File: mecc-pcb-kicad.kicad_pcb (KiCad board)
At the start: 2 copper layers, 230.1 x 130 mm, 51 parts, among them J1 UI BUS, J2 STM SIGS, J3 Wave_Gauge, J4 4.9V, J6 VESC IN, J7 IV Sens, Q1 NMOS, Q2 NMOS, Q3 PMOS, Q4 PMOS, U1 SEN-16407

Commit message: merged with Nathan's branch
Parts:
- added C1: 100 uF, Capacitor_THT:CP_Axial_L11.0mm_D5.0mm_P18.00mm_Horizontal, F.Cu at (200.9, 108.0)
- added C2: 47 uF, Capacitor_THT:CP_Axial_L11.0mm_D5.0mm_P18.00mm_Horizontal, F.Cu at (127.9, 148.6)
- added D1: 1N4007, Diode_THT:D_DO-41_SOD81_P10.16mm_Horizontal, F.Cu at (172.7, 127.0)
- added J1: UI BUS, Connector_Molex:Molex_KK-254_AE-6410-05A_1x05_P2.54mm_Vertical, F.Cu at (142.2, 119.4)
- added J2: VBatt -> 5V, Package_SIP:SIP-8_19x3mm_P2.54mm, F.Cu at (195.6, 99.1)
- added J4: 5V -> 3.3V, Package_SIP:SIP-8_19x3mm_P2.54mm, F.Cu at (195.6, 88.9)
- added J5: PDQE15-Q48-D24-D, PDQE15-Q48-D24-D:CONV_PDQE15-Q48-D24-D, F.Cu at (109.8, 179.8)
- added J8: Torq_SENS, Connector_Molex:Molex_KK-254_AE-6410-04A_1x04_P2.54mm_Vertical, F.Cu at (97.8, 148.6)
- added R1: 3k, Resistor_THT:R_Axial_DIN0204_L3.6mm_D1.6mm_P7.62mm_Horizontal, F.Cu at (97.8, 142.2)
- added R10: 50k, Resistor_THT:R_Axial_DIN0204_L3.6mm_D1.6mm_P7.62mm_Horizontal, F.Cu at (97.8, 130.8)
- added R2: 3k, Resistor_THT:R_Axial_DIN0204_L3.6mm_D1.6mm_P7.62mm_Horizontal, F.Cu at (101.6, 134.6)
- added R9: 100k, Resistor_THT:R_Axial_DIN0204_L3.6mm_D1.6mm_P7.62mm_Horizontal, F.Cu at (101.6, 123.2)
- added U2: SN74HCS09QPWRQ1, SN74HCS09QPWRQ1:SO14_PW_TEX, F.Cu at (100.3, 196.7)
- added U3: SN74LVC1G139DCUR, SN74LVC1G139DCUR:DCU0008A_N, F.Cu at (107.7, 195.1)
- J3: footprint Connector_Molex:Molex_KK-254_AE-6410-08A_1x08_P2.54mm_Vertical -> Connector_RJ:RJ45_Amphenol_RJHSE538X
- R3: value 9.8K -> 10k
- R4: value 3.9K -> 5k
- R5: value 7.45K -> 10k
- R6: value 9K -> 27k
- R7: value 6.57K -> 4.7k
- R8: value 9.8K -> 4.7k
- RHIGH_10k1, RHIGH_10k2, RHIGH_10k3, RHIGH_10k4, RHIGH_10k5, RHIGH_10k6, R_RELAY_PULLDOWN1, R_RELAY_PULLDOWN3, R_RELAY_PULLDOWN4: footprint Resistor_THT:R_Box_L14.0mm_W5.0mm_P9.00mm -> Resistor_THT:R_Axial_DIN0204_L3.6mm_D1.6mm_P7.62mm_Horizontal
- moved J7 111.9 mm to (109.2, 88.9), turned to 0 degrees
- moved R6 105.4 mm to (101.6, 86.4), turned to -90 degrees
- moved J1 98.4 mm to (153.2, 119.4)
- moved R8 65.3 mm to (120.7, 130.8)
- moved J4 65.0 mm to (120.7, 137.2), turned to 0 degrees
- moved J3 61.3 mm to (85.5, 143.8), turned to 90 degrees
- moved R3 60.5 mm to (105.4, 123.2)
- moved TP7 43.9 mm to (113.0, 137.2)
- moved JP2 43.4 mm to (124.5, 99.1), turned to -90 degrees
- moved R7 43.2 mm to (116.8, 130.8), turned to 90 degrees
- moved R4 40.5 mm to (109.2, 130.8), turned to 90 degrees
- moved R5 39.9 mm to (113.0, 130.8), turned to 90 degrees
- moved J6 38.1 mm to (83.8, 127.0)
- moved J2 19.3 mm to (142.2, 134.6)
- moved TP8 19.3 mm to (133.7, 141.7)
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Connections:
- net TORQUE_SENSOR renamed /A0
- JP2 pad 5: IO_LOW_OUT -> LOW_OUT
- JP2 pad 6: IO_HIGH_SIDE_RELAY -> HIGH_IN
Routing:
- net +5V: track 59.7 -> 207.9 mm
- net BATT_POS: track 63.2 -> 182.0 mm
- net HIGH_SIDE_STM: track 24.9 -> 133.1 mm, vias 0 -> 2
- net PRE_LOW_DIS_STM: track 52.9 -> 149.8 mm
- net IO_HIGH_SIDE_RELAY: track 78.5 -> 0.00 mm
- net IO_LOW_OUT: track 71.9 -> 0.00 mm
- net /A3: track 87.3 -> 28.5 mm
- net GND: track 748.4 -> 806.2 mm
- net VESC_OUTPUT: track 43.5 -> 92.3 mm
- net HIGH_SIDE: track 92.4 -> 46.8 mm
- net VESC_INPUT: track 43.5 -> 83.3 mm
- net HIGH_IN: track 0.00 -> 35.7 mm
- net IO_ESTOP: track 74.4 -> 40.5 mm
- net PRE_LOW_DIS: track 162.3 -> 195.1 mm
- net LOW_OUT: track 0.00 -> 32.1 mm
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- removed copper zone on B.Cu, net GND
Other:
- board text added: "USB C THIS <-- WAY"
- board text added: "WEC-PROTOTYPE PCB MK2 FA'23 Kelvin Resch (kr562) Nathan Rakhlin (npr29)"
- board text removed: "USB C THIS WAY ->"

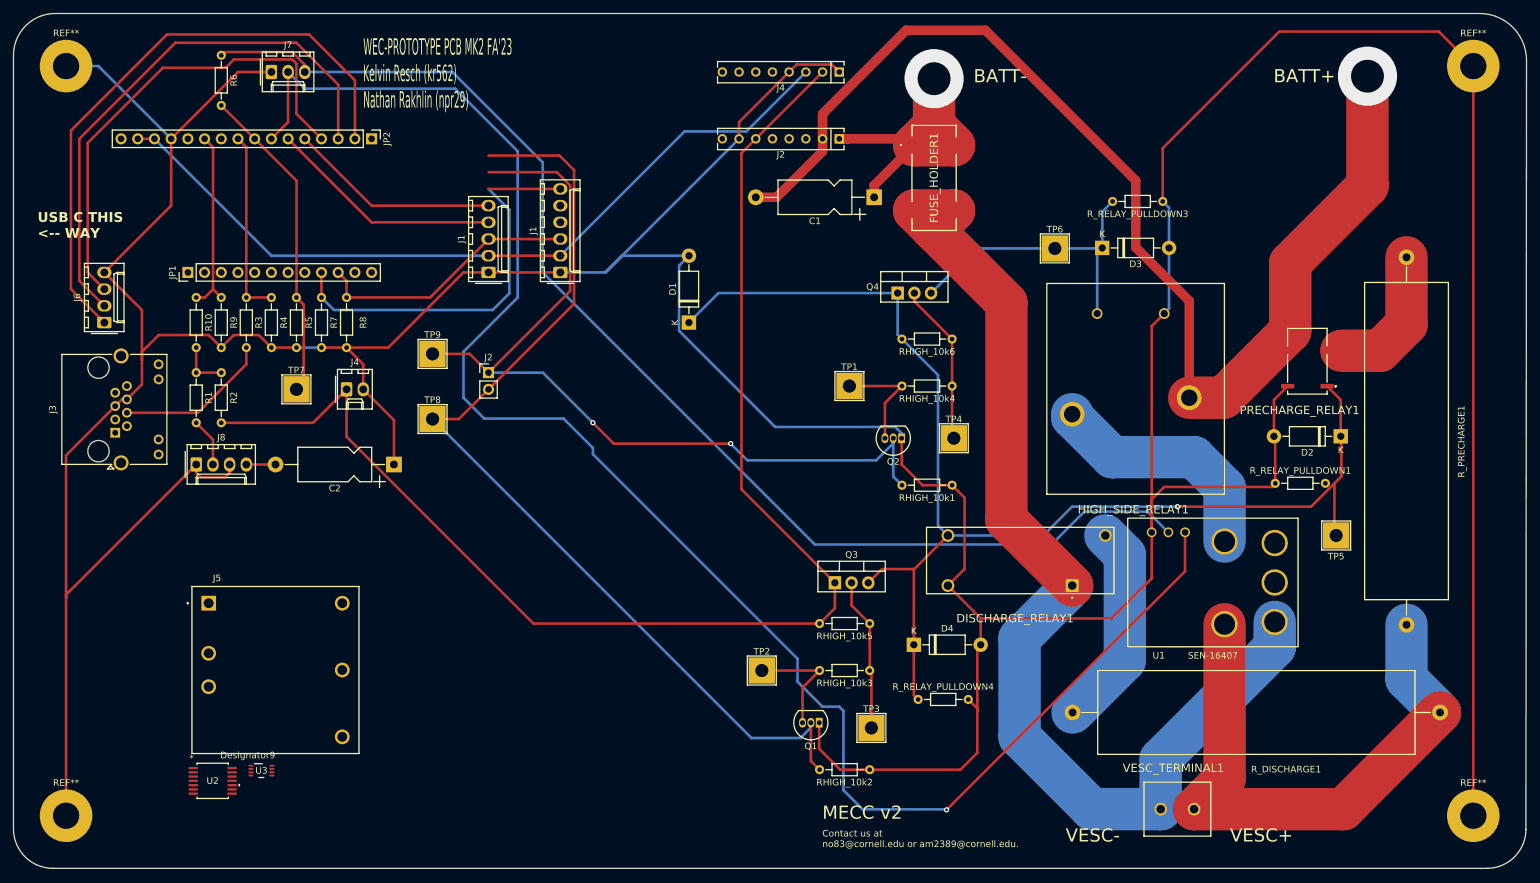
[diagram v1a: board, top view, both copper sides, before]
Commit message: Implemented all of list except for CMOS stuff
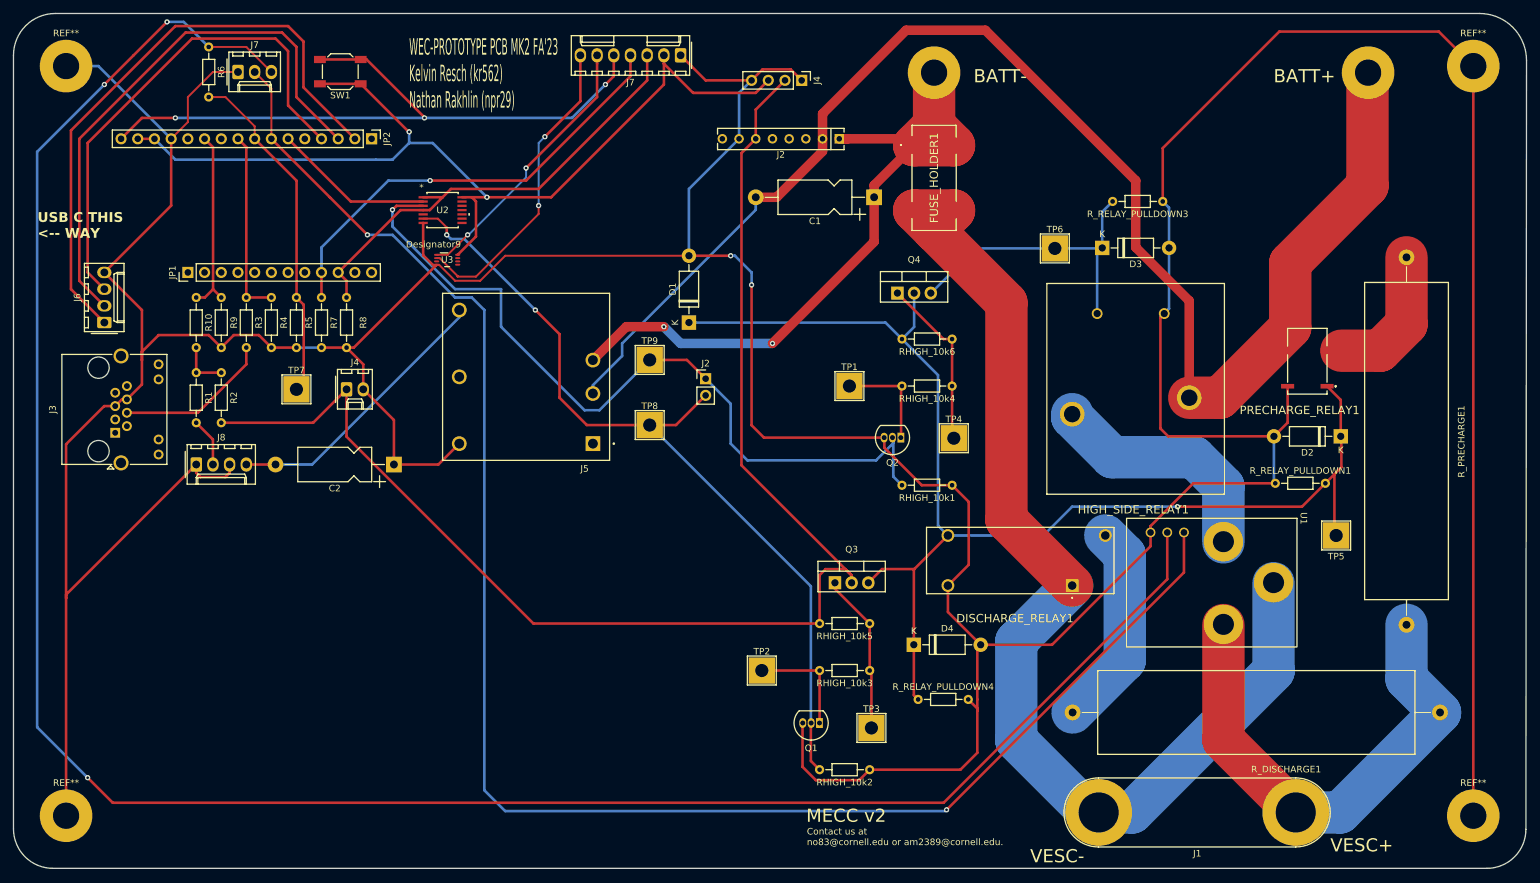
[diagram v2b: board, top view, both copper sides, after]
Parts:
- removed the J1 at (153.2, 119.4)
- removed the J1 at (142.2, 119.4)
- removed VESC_TERMINAL1: TB006-508-02BE, MECC-CUI-Screw-terminal:TB00650802BE
- added ?: , , F.Cu at (276.0, 89.0)
- added ?: , , F.Cu at (210.0, 89.0)
- added J1: VESC Term, Connector:Banana_Jack_2Pin, F.Cu at (265.0, 201.5)
- added J7: UI BUS, Connector_Molex:Molex_KK-254_AE-6410-07A_1x07_P2.54mm_Vertical, F.Cu at (171.4, 86.4)
- added SW1: Reset, Button_Switch_SMD:SW_SPST_SKQG_WithoutStem, F.Cu at (119.7, 88.8)
- J4: footprint Package_SIP:SIP-8_19x3mm_P2.54mm -> Connector_PinHeader_2.54mm:PinHeader_1x04_P2.54mm_Vertical
- Q1, Q2: footprint Package_TO_SOT_THT:TO-92_Inline -> Library:WEC_NMOS
- Q3, Q4: footprint Package_TO_SOT_THT:TO-220-3_Vertical -> Library:WEC_PMOS
- R7, R8: value 4.7k -> 10k
- moved U2 93.6 mm to (135.3, 109.9)
- moved U3 82.7 mm to (135.9, 117.5)
- moved J5 58.7 mm to (148.0, 135.3), turned to 180 degrees
- moved TP8 33.0 mm to (166.8, 142.6)
- moved TP9 33.0 mm to (166.8, 132.7)
- moved J2 33.0 mm to (175.3, 135.5)
- moved J4 5.85 mm to (189.9, 90.2), turned to -90 degrees
- moved J7 5.08 mm to (104.1, 88.9)
- moved Q3 2.55 mm to (197.5, 166.6)
- moved Q4 2.50 mm to (207.0, 122.5)
- moved R6 2.29 mm to (99.7, 85.1)
- moved Q2 1.40 mm to (203.7, 144.5)
- moved Q1 1.23 mm to (191.3, 187.9)
- moved U1 0.17 mm to (265.2, 156.8)
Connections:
- U1 pad 2: unconnected-(U1-GND-Pad2) -> VESC_NEG
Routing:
- net BATT_V_SENSOR: track 189.1 -> 332.2 mm, vias 0 -> 3
- net RESET: track 0.00 -> 101.7 mm, vias 0 -> 3
- net BATT_NEG: track 45.2 -> 104.3 mm, vias 1 -> 2
- net TORQ_SWITCH_2: track 0.00 -> 47.4 mm, vias 0 -> 2
- net TORQ_SWITCH_1: track 0.00 -> 41.5 mm, vias 0 -> 2
- net BATT_POS: track 182.0 -> 221.8 mm, vias 1 -> 0
- net +24V: track 4.45 -> 42.8 mm
- net LOW_OUT: track 32.1 -> 0.00 mm
- net IO_ESTOP: track 40.5 -> 70.2 mm
- net +3.3V: track 120.5 -> 149.2 mm, vias 0 -> 2
- net GND: track 806.2 -> 833.8 mm, vias 0 -> 2
- net PRE_LOW_DIS_STM: track 149.8 -> 127.3 mm, vias 0 -> 2
- net VESC_POS: track 89.0 -> 76.7 mm
- net HIGH_SIDE_STM: track 133.1 -> 121.1 mm, vias 2 -> 1
- net HIGH_IN: track 35.7 -> 24.5 mm
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
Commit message: Implemented some of becca's changes
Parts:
- 5V -> 3.3V: renamed from J4
- IV Sens: renamed from J7
- Torq Sensor: renamed from J8
- UI Bus: renamed from J7; footprint Connector_Molex:Molex_KK-254_AE-6410-07A_1x07_P2.54mm_Vertical -> Connector_Molex:Molex_KK-254_AE-6410-08A_1x08_P2.54mm_Vertical
- VBatt -> 5V: renamed from J2
- VESC IN: renamed from J6
- Wave Gauge: renamed from J3
- moved Wave Gauge 14.0 mm to (84.4, 157.7)
- moved VESC IN 11.5 mm to (83.8, 138.5)
- moved D3 6.69 mm to (235.5, 109.0)
- moved HIGH_SIDE_RELAY1 6.69 mm to (230.9, 134.2)
- moved TP6 6.69 mm to (228.3, 109.0)
- moved R_RELAY_PULLDOWN3 6.69 mm to (244.7, 101.9)
- renumbered REF** to GND, SW1 to Reset
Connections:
- JP1 pad 5: /D12 -> Torq_SW_Mode_1
- JP1 pad 6: /D11 -> Torq_SW_Mode_2
- JP1 pad 7: /D10 -> Torq_SW_Mode_3
- JP1 pad 8: /D9 -> Ref_Model_SW
- JP2 pad 5: LOW_OUT -> LOW_IN
- U3 pad 5: unconnected-(U3-Y2-Pad5) -> Torq_SW_Mode_3
- U3 pad 6: unconnected-(U3-Y1-Pad6) -> Torq_SW_Mode_2
- U3 pad 7: unconnected-(U3-Y0-Pad7) -> Torq_SW_Mode_1
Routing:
- net Ref_Model_SW: track 0.00 -> 55.6 mm, vias 0 -> 1
- net Torq_SW_Mode_1: track 0.00 -> 48.8 mm, vias 0 -> 1
- net Torq_SW_Mode_2: track 0.00 -> 43.1 mm, vias 0 -> 1
- net Torq_SW_Mode_3: track 0.00 -> 31.1 mm, vias 0 -> 1
- net LOW_IN: track 0.00 -> 24.9 mm, vias 0 -> 2
- net /A4: track 52.4 -> 73.1 mm, vias 0 -> 2
- net /A3: track 28.5 -> 42.8 mm
- net VESC_POWER_SWITCH: track 76.6 -> 89.1 mm
- net VESC_INPUT: track 84.2 -> 96.4 mm
- net WAVE_GAUGE: track 23.8 -> 35.7 mm
- net VESC_OUTPUT: track 92.3 -> 103.8 mm
- net /A1: track 28.3 -> 35.6 mm
- net +3.3V: track 149.2 -> 155.9 mm
- net BATT_CURR_SENSOR: track 256.1 -> 261.3 mm
- net BATT_V_SENSOR: track 332.2 -> 328.0 mm
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
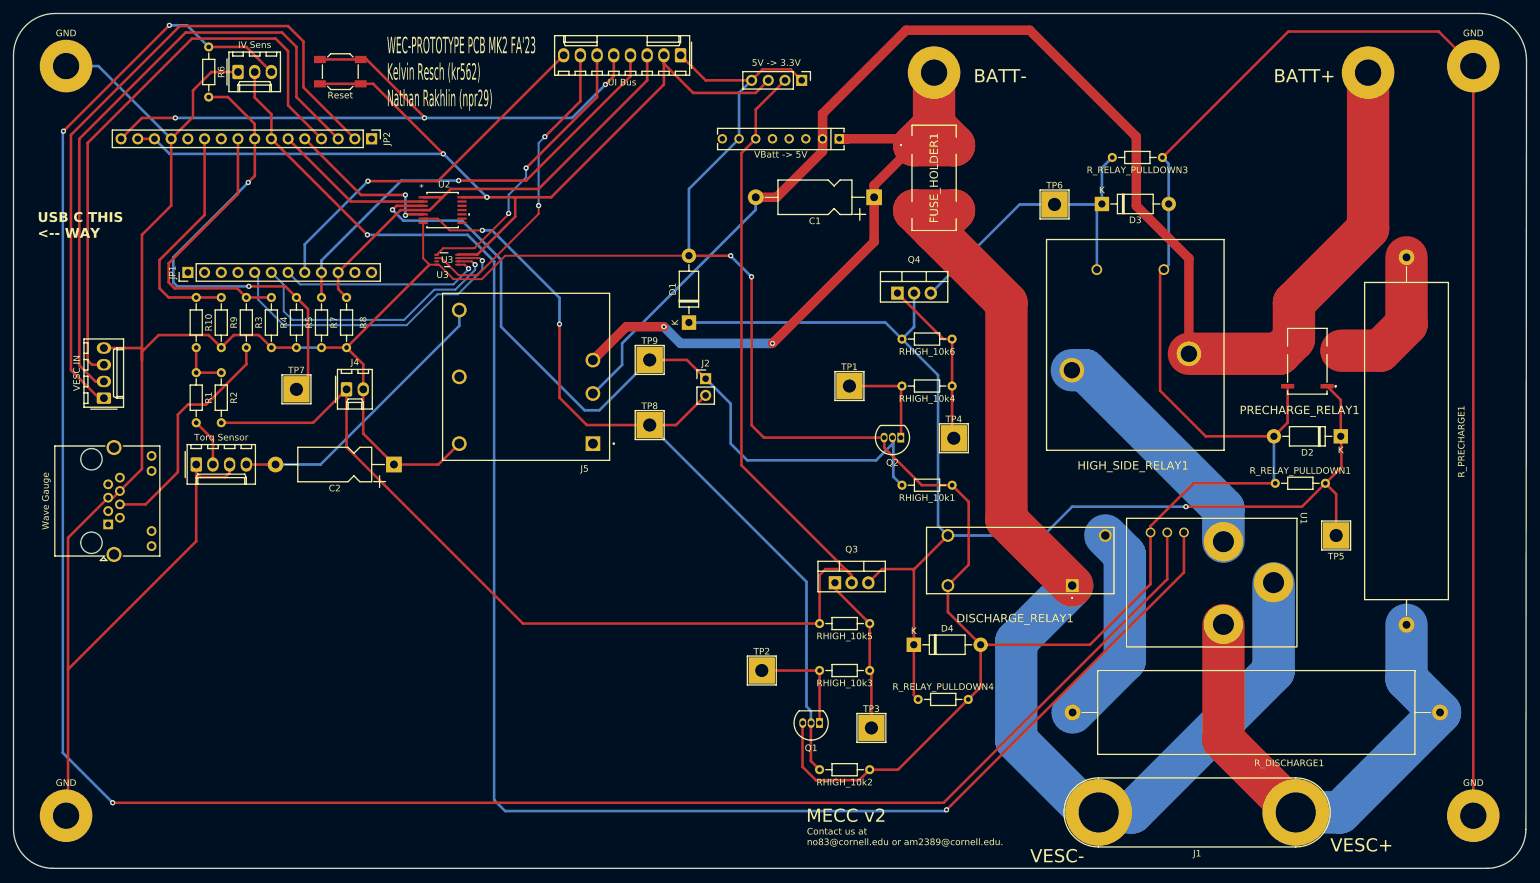
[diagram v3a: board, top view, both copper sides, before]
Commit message: Added a PGND and AGND connection, and cleaned up some routing.
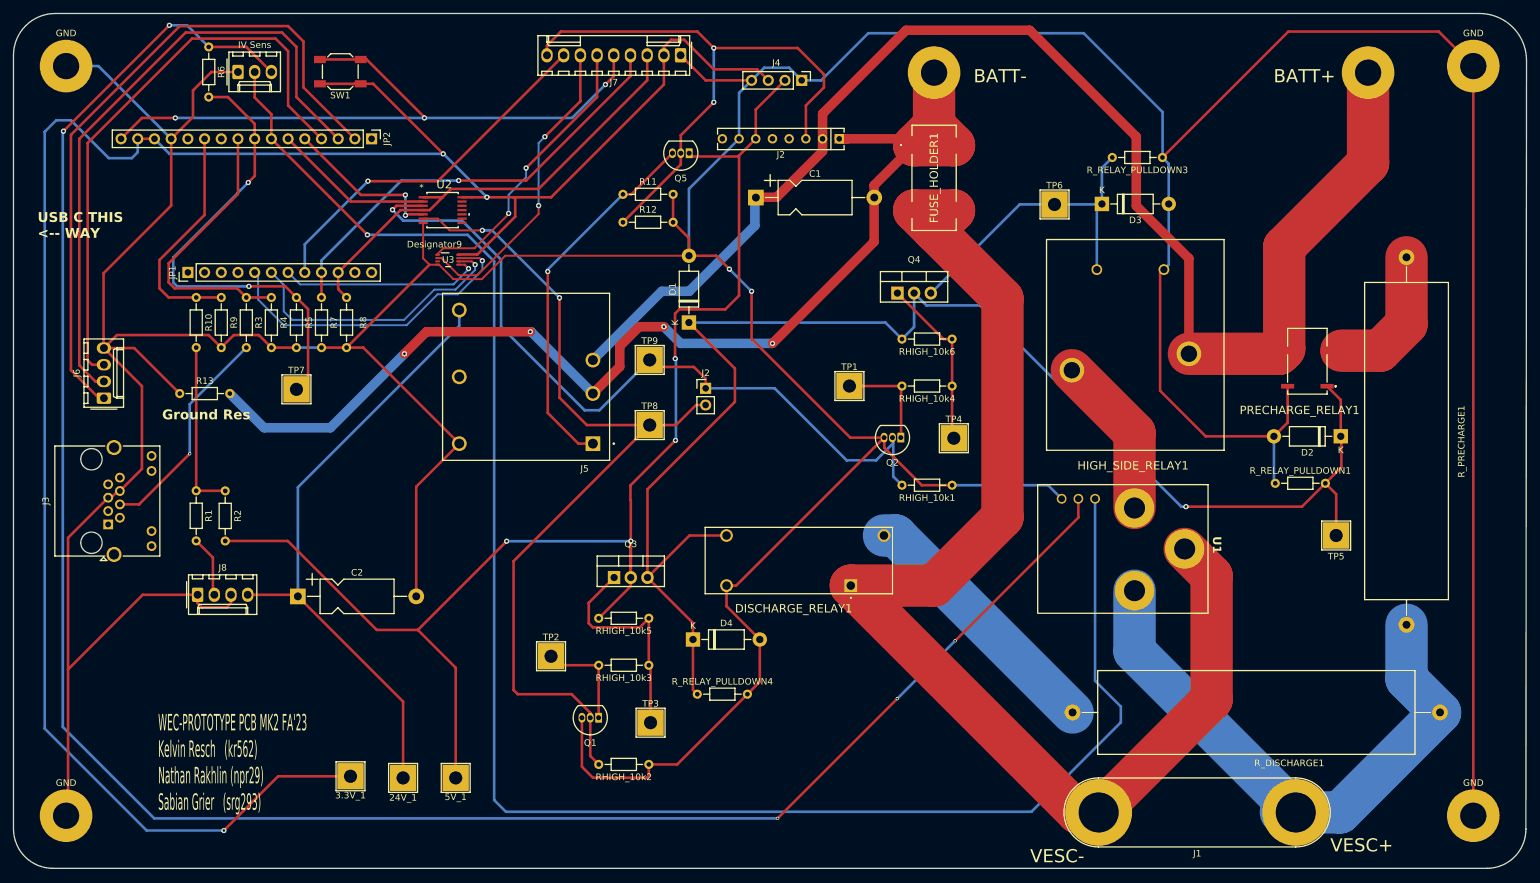
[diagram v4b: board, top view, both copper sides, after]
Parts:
- removed the J4 at (120.7, 137.2)
- added 24V_1: TestPoint, TestPoint:TestPoint_THTPad_4.0x4.0mm_Drill2.0mm, F.Cu at (129.2, 196.2)
- added 3.3V_1: TestPoint, TestPoint:TestPoint_THTPad_4.0x4.0mm_Drill2.0mm, F.Cu at (121.2, 196.0)
- added 5V_1: TestPoint, TestPoint:TestPoint_THTPad_4.0x4.0mm_Drill2.0mm, F.Cu at (137.2, 196.2)
- added Q5: NMOS, Library:WEC_NMOS, F.Cu at (171.5, 101.2)
- added R11: 10k, Resistor_THT:R_Axial_DIN0204_L3.6mm_D1.6mm_P7.62mm_Horizontal, F.Cu at (162.7, 107.5)
- added R12: 10k, Resistor_THT:R_Axial_DIN0204_L3.6mm_D1.6mm_P7.62mm_Horizontal, F.Cu at (162.7, 111.8)
- added R13: 0, Resistor_THT:R_Axial_DIN0204_L3.6mm_D1.6mm_P7.62mm_Horizontal, F.Cu at (95.3, 137.8)
- J2: renamed from VBatt -> 5V
- J3: renamed from Wave Gauge
- J4: renamed from 5V -> 3.3V
- J6: renamed from VESC IN
- J7: renamed from UI Bus; footprint Connector_Molex:Molex_KK-254_AE-6410-08A_1x08_P2.54mm_Vertical -> Connector_Molex:Molex_KK-254_AE-6410-09A_1x09_P2.54mm_Vertical
- J8: renamed from Torq Sensor
- moved DISCHARGE_RELAY1 33.7 mm to (197.3, 167.0)
- moved Q1 33.6 mm to (157.7, 187.1)
- moved Q3 33.6 mm to (163.9, 165.8)
- moved RHIGH_10k2 33.6 mm to (166.6, 194.2)
- moved RHIGH_10k3 33.6 mm to (166.6, 179.1)
- moved RHIGH_10k5 33.6 mm to (166.6, 172.0)
- moved TP3 33.6 mm to (166.9, 187.8)
- moved D4 33.6 mm to (173.3, 175.2)
- moved R_RELAY_PULLDOWN4 33.6 mm to (174.0, 183.5)
- moved TP2 32.1 mm to (151.8, 177.8)
- moved C2 24.8 mm to (113.2, 168.6), turned to 0 degrees
- moved J8 19.8 mm to (98.0, 168.4)
- moved R2 18.0 mm to (102.2, 152.6)
- moved C1 18.0 mm to (182.9, 108.0), turned to 0 degrees
- moved R1 18.0 mm to (97.8, 160.2)
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- renumbered Reset to SW1
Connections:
- C1 pad 1: BATT_NEG -> BATT_POS
- C1 pad 2: BATT_POS -> BATT_NEG
- C2 pad 1: GND -> +24V
- C2 pad 2: +24V -> GND
- J2 pad 3: unconnected-(J2-Pin_3-Pad3) -> DCDC_SW
- J5 pad 1: unconnected-(J5-CTRL-Pad1) -> Net-(J5-CTRL)
- J5 pad 2: BATT_POS -> BATT_NEG
- J5 pad 3: BATT_NEG -> BATT_POS
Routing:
- net +3.3V: track 155.9 -> 324.3 mm, vias 2 -> 3
- net DCDC_SW: track 0.00 -> 90.3 mm, vias 0 -> 2
- net BATT_NEG: track 104.3 -> 175.5 mm, vias 2 -> 4
- net GND: track 835.5 -> 900.6 mm
- net Net-(J5-CTRL): track 0.00 -> 56.9 mm, vias 0 -> 1
- net +24V: track 44.6 -> 97.3 mm
- net PRE_LOW_DIS: track 195.5 -> 227.0 mm
- net VESC_NEG: track 170.3 -> 190.8 mm
- net Net-(R1-Pad2): track 7.62 -> 26.2 mm
- net BATT_V_SENSOR: track 328.0 -> 313.9 mm, vias 3 -> 5
- net VESC_POS: track 76.7 -> 89.8 mm
- net Net-(HIGH_SIDE_RELAY1-NO): track 36.8 -> 24.9 mm
- net BATT_CURR_SENSOR: track 261.3 -> 272.0 mm, vias 2 -> 1
- net Net-(Q3-G): track 24.4 -> 34.5 mm
- net Net-(DISCHARGE_RELAY1-NC): track 31.4 -> 39.8 mm
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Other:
- board text added: "Ground Res"
- board text added: "WEC-PROTOTYPE PCB MK2 FA'23 Kelvin Resch (kr562) Nathan Rakhlin (npr29) Sabian Grier (srg293)"
- board text removed: "Contact us at no83@cornell.edu or am2389@cornell.edu."
- board text removed: "MECC v2"
- board text removed: "WEC-PROTOTYPE PCB MK2 FA'23 Kelvin Resch (kr562) Nathan Rakhlin (npr29)"
